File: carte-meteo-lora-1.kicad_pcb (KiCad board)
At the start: 2 copper layers, 118 parts, among them J1 TC2030, J2 Conn_01x04, J3 Conn_01x04, J4 Conn_Coaxial, J5 USB_C_Receptacle_USB2.0_14P, J6 Solar_Cell, J7 Conn_01x02, J8 Battery_Cell, Q1 AO4882, Q2 AO4882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

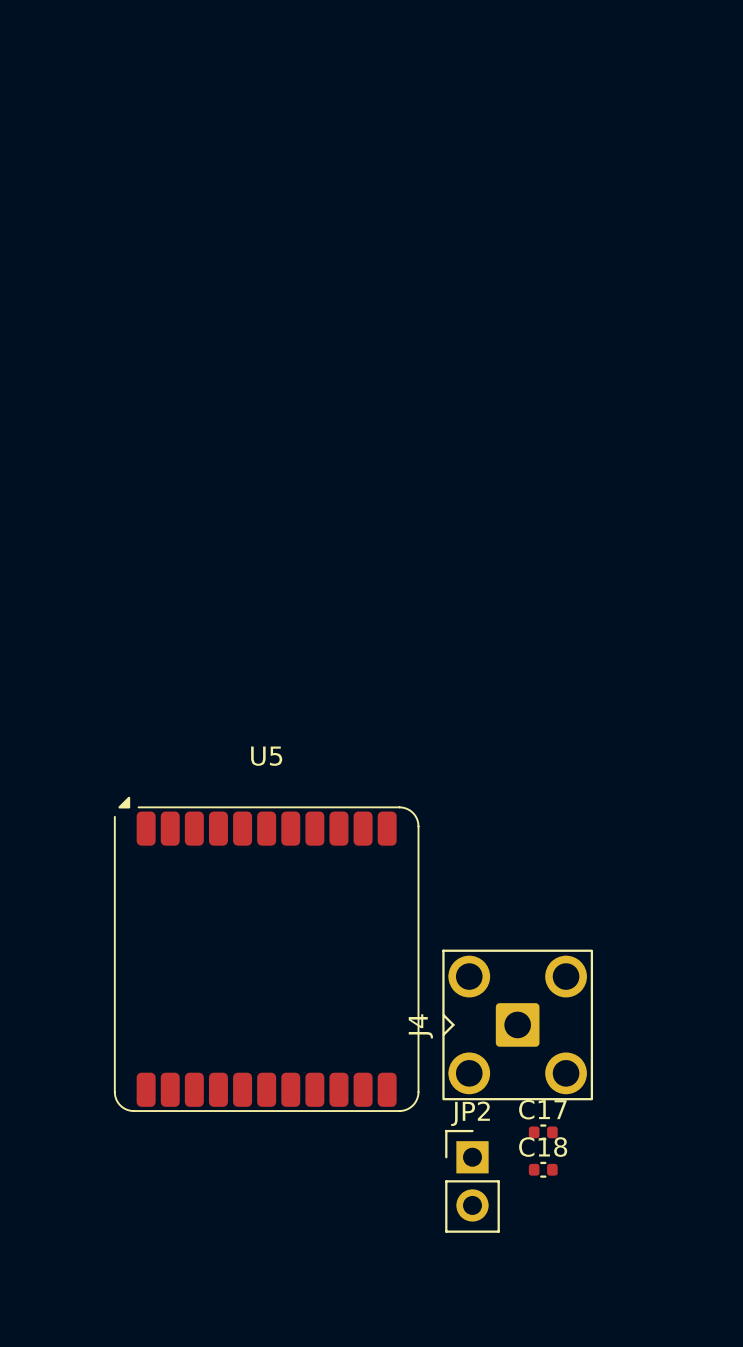
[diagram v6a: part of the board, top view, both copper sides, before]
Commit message: pcb: add lora layout
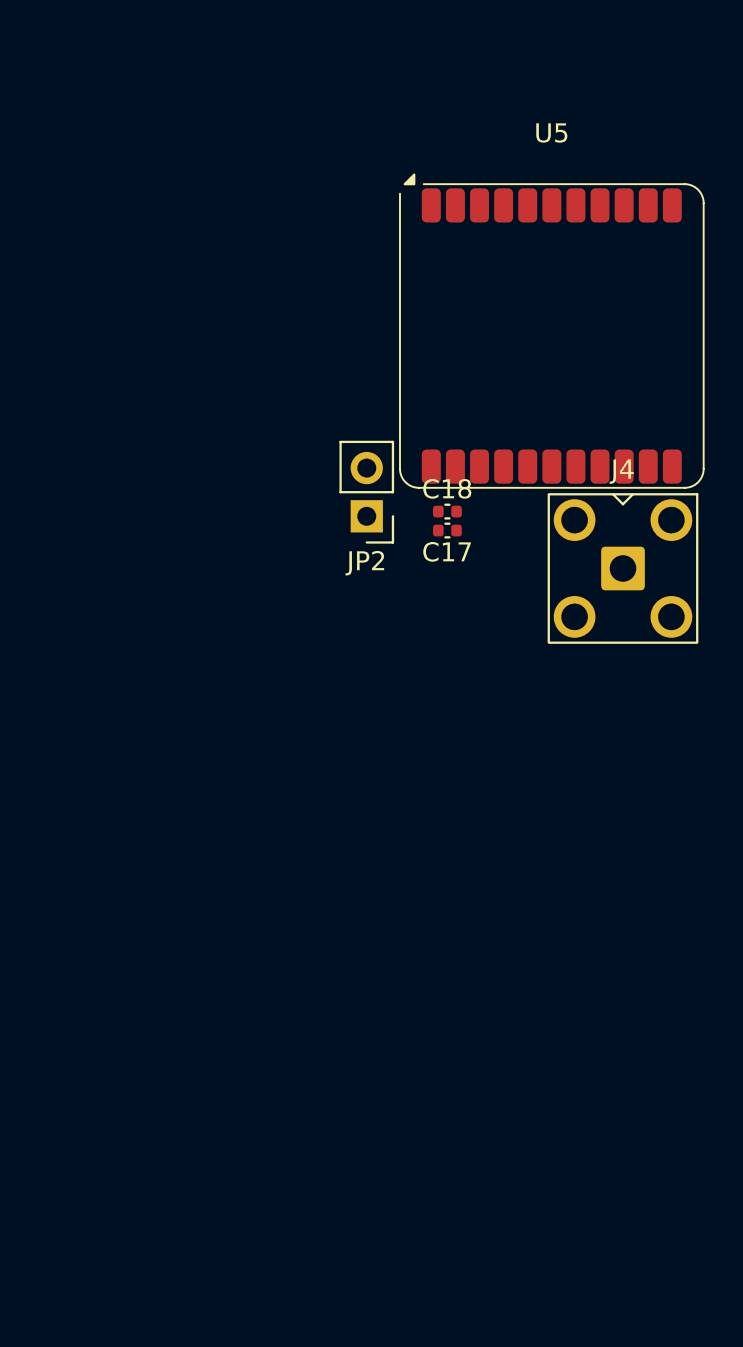
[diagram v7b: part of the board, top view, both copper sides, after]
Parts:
- moved U5 36.1 mm to (199.2, 82.2)
- moved C18 35.0 mm to (193.8, 91.5)
- moved JP2 34.2 mm to (189.5, 91.8), turned to 180 degrees
- moved C17 32.1 mm to (193.8, 92.5), turned to 180 degrees
- moved J4 24.7 mm to (203.0, 94.5), turned to -90 degrees
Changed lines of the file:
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@@
 	(footprint "GLCS:Silicontra_SX1262ZTR8"
 		(layer "F.Cu")
-		(at 184.225 115.085)
+		(at 199.25 82.25)
 		(descr "Silicontra SX1262ZTR8 LoRa Module")
 		(tags "LoRa Silicontra SX1262ZTR8")
@@
 	(footprint "Connector_Coaxial:SMA_BAT_Wireless_BWSMA-KWE-Z001"
 		(layer "F.Cu")
-		(at 197.45 118.55)
+		(at 203 94.5 -90)
 		(descr "BAT Wireless BWSMA-KWE-Z00 https://www.lcsc.com/datasheet/lcsc_datasheet_2310171703_BAT-WIRELESS-BWSMA-KWE-Z001_C496551.pdf")
 		(tags "SMA THT Female Jack Horizontal")
 		(property "Reference" "J4"
-			(at -5.2 0 90)
+			(at -5.2 0 0)
 			(layer "F.SilkS")
 			(effects
@@
 		)
 		(property "Value" "Conn_Coaxial"
-			(at 0 5 0)
+			(at 0 5 90)
 			(layer "F.Fab")
 			(effects
@@
 		)
 		(property "Datasheet" ""
-			(at 0 0 0)
+			(at 0 0 270)
 			(unlocked yes)
 			(layer "F.Fab")
@@
 		)
 		(property "Description" "coaxial connector (BNC, SMA, SMB, SMC, Cinch/RCA, LEMO, ...)"
-			(at 0 0 0)
+			(at 0 0 270)
 			(unlocked yes)
 			(layer "F.Fab")
@@
 		)
 		(property "Basic" "Z"
-			(at 0 0 0)
+			(at 0 0 270)
 			(unlocked yes)
 			(layer "F.Fab")
@@
 		)
 		(property "JLCPCB Part #" "C496551"
-			(at 0 0 0)
+			(at 0 0 270)
 			(unlocked yes)
 			(layer "F.Fab")
@@
 		)
 		(property "Manufacturer" "BAT WIRELESS"
-			(at 0 0 0)
+			(at 0 0 270)
 			(unlocked yes)
 			(layer "F.Fab")
@@
 		)
 		(property "Manufacturer Part Number" "BWSMA-KWE-Z001"
-			(at 0 0 0)
+			(at 0 0 270)
 			(unlocked yes)
 			(layer "F.Fab")
@@
 		)
 		(fp_line
-			(start -3 -9.5)
-			(end 3 -10)
+			(start -3 3)
+			(end 3 3)
 			(stroke
 				(width 0.1)
@@
 		)
 		(fp_line
-			(start -3 -9)
-			(end 3 -9.5)
+			(start -2 0)
+			(end -3 1)
 			(stroke
 				(width 0.1)
@@
 		)
 		(fp_line
-			(start -3 -8.5)
-			(end 3 -9)
+			(start -3 -1)
+			(end -2 0)
 			(stroke
 				(width 0.1)
@@
 		)
 		(fp_line
-			(start -3 -8)
-			(end 3 -8.5)
+			(start -3 -3)
+			(end -3 3)
 			(stroke
 				(width 0.1)
@@
 		)
 		(fp_line
-			(start -3 -7.5)
-			(end 3 -8)
+			(start -3 -3)
+			(end 3 -3)
 			(stroke
 				(width 0.1)
@@
 		)
 		(fp_line
-			(start -3 -7)
-			(end 3 -7.5)
+			(start 3 -3)
+			(end 3 3)
 			(stroke
 				(width 0.1)
@@
 		)
 		(fp_line
-			(start -3 -3)
-			(end -3 3)
+			(start -3 -7)
+			(end 3 -7.5)
 			(stroke
 				(width 0.1)
@@
 		)
 		(fp_line
-			(start -3 -3)
-			(end 3 -3)
+			(start -3 -7.5)
+			(end 3 -8)
 			(stroke
 				(width 0.1)
@@
 		)
 		(fp_line
-			(start -3 -1)
-			(end -2 0)
+			(start -3 -8)
+			(end 3 -8.5)
 			(stroke
 				(width 0.1)
@@
 		)
 		(fp_line
-			(start -3 3)
-			(end 3 3)
+			(start -3 -8.5)
+			(end 3 -9)
 			(stroke
 				(width 0.1)
@@
 		)
 		(fp_line
-			(start -2.5 -11.5)
-			(end -2.5 -3)
+			(start -3 -9)
+			(end 3 -9.5)
 			(stroke
 				(width 0.1)
@@
 		)
 		(fp_line
-			(start -2.5 -11.5)
-			(end 2.5 -11.5)
+			(start -3 -9.5)
+			(end 3 -10)
 			(stroke
 				(width 0.1)
@@
 		)
 		(fp_line
-			(start -2 0)
-			(end -3 1)
+			(start -2.5 -11.5)
+			(end -2.5 -3)
 			(stroke
 				(width 0.1)
@@
 		)
 		(fp_line
-			(start 2.5 -11.5)
-			(end 2.5 -3)
+			(start -2.5 -11.5)
+			(end 2.5 -11.5)
 			(stroke
 				(width 0.1)
@@
 		)
 		(fp_line
-			(start 3 -3)
-			(end 3 3)
+			(start 2.5 -11.5)
+			(end 2.5 -3)
 			(stroke
 				(width 0.1)
@@
 		)
 		(fp_text user "${REFERENCE}"
-			(at 0 0 0)
+			(at 0 0 90)
 			(layer "F.Fab")
 			(effects
@@
 		)
 		(pad "1" thru_hole roundrect
-			(at 0 0)
+			(at 0 0 270)
 			(size 2.3 2.3)
 			(drill 1.4)
@@
 		)
 		(pad "2" thru_hole circle
-			(at -2.55 -2.55)
+			(at -2.55 -2.55 270)
 			(size 2.2 2.2)
 			(drill 1.4)
@@
 		)
 		(pad "2" thru_hole circle
-			(at -2.55 2.55)
+			(at -2.55 2.55 270)
 			(size 2.2 2.2)
 			(drill 1.4)
@@
 		)
 		(pad "2" thru_hole circle
-			(at 2.55 -2.55)
+			(at 2.55 -2.55 270)
 			(size 2.2 2.2)
 			(drill 1.4)
@@
 		)
 		(pad "2" thru_hole circle
-			(at 2.55 2.55)
+			(at 2.55 2.55 270)
 			(size 2.2 2.2)
 			(drill 1.4)
@@
 	(footprint "Capacitor_SMD:C_0402_1005Metric"
 		(layer "F.Cu")
-		(at 198.8 124.21)
+		(at 193.75 92.5 180)
 		(descr "Capacitor SMD 0402 (1005 Metric), square (rectangular) end terminal, IPC-7351 nominal, (Body size source: IPC-SM-782 page 76, https://www.pcb-3d.com/wordpress/wp-content/uploads/ipc-sm-782a_amendment_1_and_2.pdf)")
 		(tags "capacitor")
@@
 		)
 		(property "Manufacturer" "Samsung Electro-Mechanics "
-			(at 0 0 0)
+			(at 0 0 180)
 			(unlocked yes)
 			(layer "F.Fab")
@@
 		)
 		(property "Manufacturer Part Number" "CL05A106MQ5NUNC"
-			(at 0 0 0)
+			(at 0 0 180)
 			(unlocked yes)
 			(layer "F.Fab")
@@
 		)
 		(property "Basic" "Y"
-			(at 0 0 0)
+			(at 0 0 180)
 			(unlocked yes)
 			(layer "F.Fab")
@@
 		)
 		(property "JLCPCB Part #" "C15525"
-			(at 0 0 0)
+			(at 0 0 180)
 			(unlocked yes)
 			(layer "F.Fab")
@@
 		(duplicate_pad_numbers_are_jumpers no)
 		(fp_line
-			(start -0.107836 -0.36)
-			(end 0.107836 -0.36)
+			(start -0.107836 0.36)
+			(end 0.107836 0.36)
 			(stroke
 				(width 0.12)
@@
 		)
 		(fp_line
-			(start -0.107836 0.36)
-			(end 0.107836 0.36)
+			(start -0.107836 -0.36)
+			(end 0.107836 -0.36)
 			(stroke
 				(width 0.12)
@@
 		)
 		(pad "1" smd roundrect
-			(at -0.48 0)
+			(at -0.48 0 180)
 			(size 0.56 0.62)
 			(layers "F.Cu" "F.Mask" "F.Paste")
@@
 		)
 		(pad "2" smd roundrect
-			(at 0.48 0)
+			(at 0.48 0 180)
 			(size 0.56 0.62)
 			(layers "F.Cu" "F.Mask" "F.Paste")
@@
 	(footprint "Capacitor_SMD:C_0402_1005Metric"
 		(layer "F.Cu")
-		(at 198.8 126.18)
+		(at 193.75 91.5)
 		(descr "Capacitor SMD 0402 (1005 Metric), square (rectangular) end terminal, IPC-7351 nominal, (Body size source: IPC-SM-782 page 76, https://www.pcb-3d.com/wordpress/wp-content/uploads/ipc-sm-782a_amendment_1_and_2.pdf)")
 		(tags "capacitor")
@@
 	(footprint "Connector_PinHeader_2.54mm:PinHeader_1x02_P2.54mm_Vertical"
 		(layer "F.Cu")
-		(at 195.07 125.52)
+		(at 189.5 91.75 180)
 		(descr "Through hole straight pin header, 1x02, 2.54mm pitch, single row")
 		(tags "Through hole pin header THT 1x02 2.54mm single row")
@@
 		)
 		(fp_line
-			(start -1.38 -1.38)
-			(end 0 -1.38)
+			(start 1.38 1.27)
+			(end 1.38 3.92)
 			(stroke
 				(width 0.12)
@@
 		)
 		(fp_line
-			(start -1.38 0)
-			(end -1.38 -1.38)
+			(start -1.38 3.92)
+			(end 1.38 3.92)
 			(stroke
 				(width 0.12)
@@
 		(fp_line
 			(start -1.38 1.27)
-			(end -1.38 3.92)
+			(end 1.38 1.27)
 			(stroke
 				(width 0.12)
@@
 		(fp_line
 			(start -1.38 1.27)
-			(end 1.38 1.27)
+			(end -1.38 3.92)
 			(stroke
 				(width 0.12)
@@
 		)
 		(fp_line
-			(start -1.38 3.92)
-			(end 1.38 3.92)
+			(start -1.38 0)
+			(end -1.38 -1.38)
 			(stroke
 				(width 0.12)
@@
 		)
 		(fp_line
-			(start 1.38 1.27)
-			(end 1.38 3.92)
+			(start -1.38 -1.38)
+			(end 0 -1.38)
 			(stroke
 				(width 0.12)
@@
 		)
 		(fp_line
-			(start -1.27 -0.635)
-			(end -0.635 -1.27)
+			(start 1.27 3.81)
+			(end -1.27 3.81)
 			(stroke
 				(width 0.1)
@@
 		)
 		(fp_line
-			(start -1.27 3.81)
-			(end -1.27 -0.635)
+			(start 1.27 -1.27)
+			(end 1.27 3.81)
 			(stroke
 				(width 0.1)
@@
 		)
 		(fp_line
-			(start 1.27 -1.27)
-			(end 1.27 3.81)
+			(start -1.27 3.81)
+			(end -1.27 -0.635)
 			(stroke
 				(width 0.1)
@@
 		)
 		(fp_line
-			(start 1.27 3.81)
-			(end -1.27 3.81)
+			(start -1.27 -0.635)
+			(end -0.635 -1.27)
 			(stroke
 				(width 0.1)
@@
 		)
 		(pad "1" thru_hole rect
-			(at 0 0)
+			(at 0 0 180)
 			(size 1.7 1.7)
 			(drill 1)
@@
 		)
 		(pad "2" thru_hole circle
-			(at 0 2.54)
+			(at 0 2.54 180)
 			(size 1.7 1.7)
 			(drill 1)

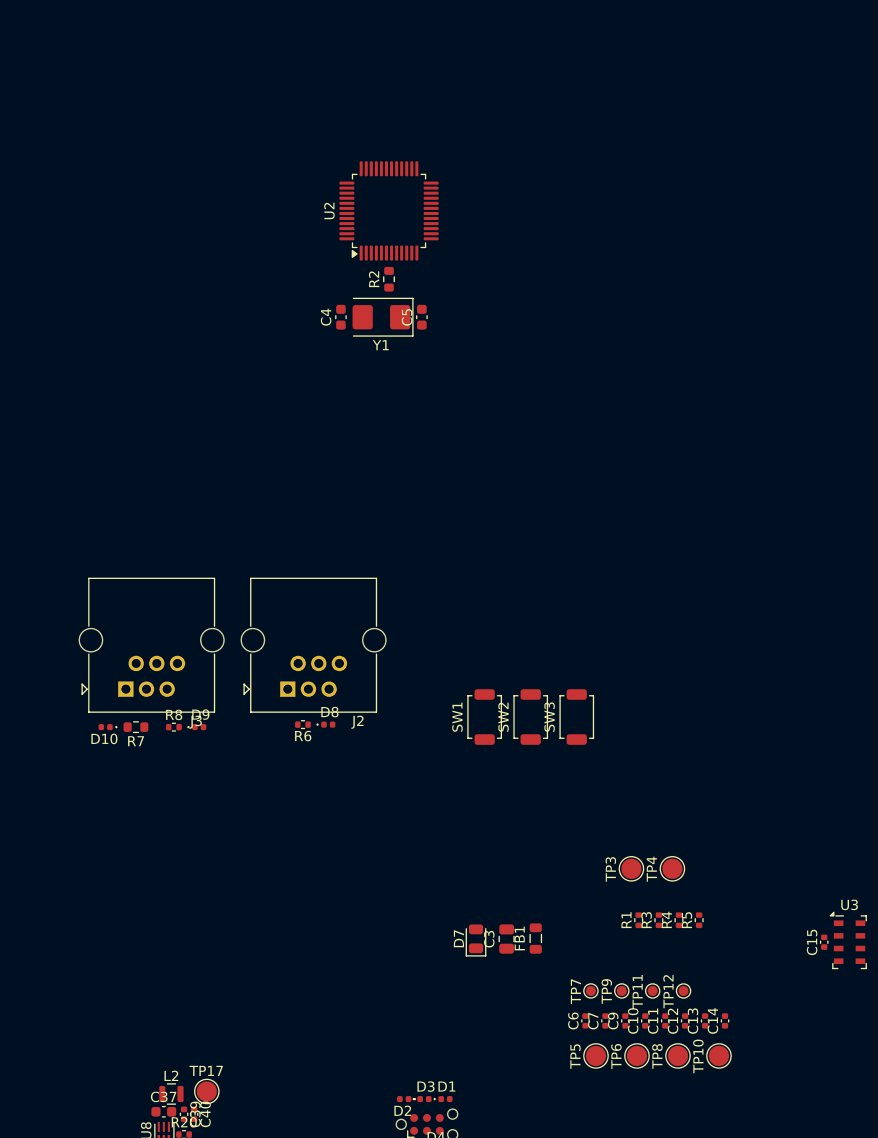
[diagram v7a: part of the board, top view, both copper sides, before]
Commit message: pcb: add stm32 layout
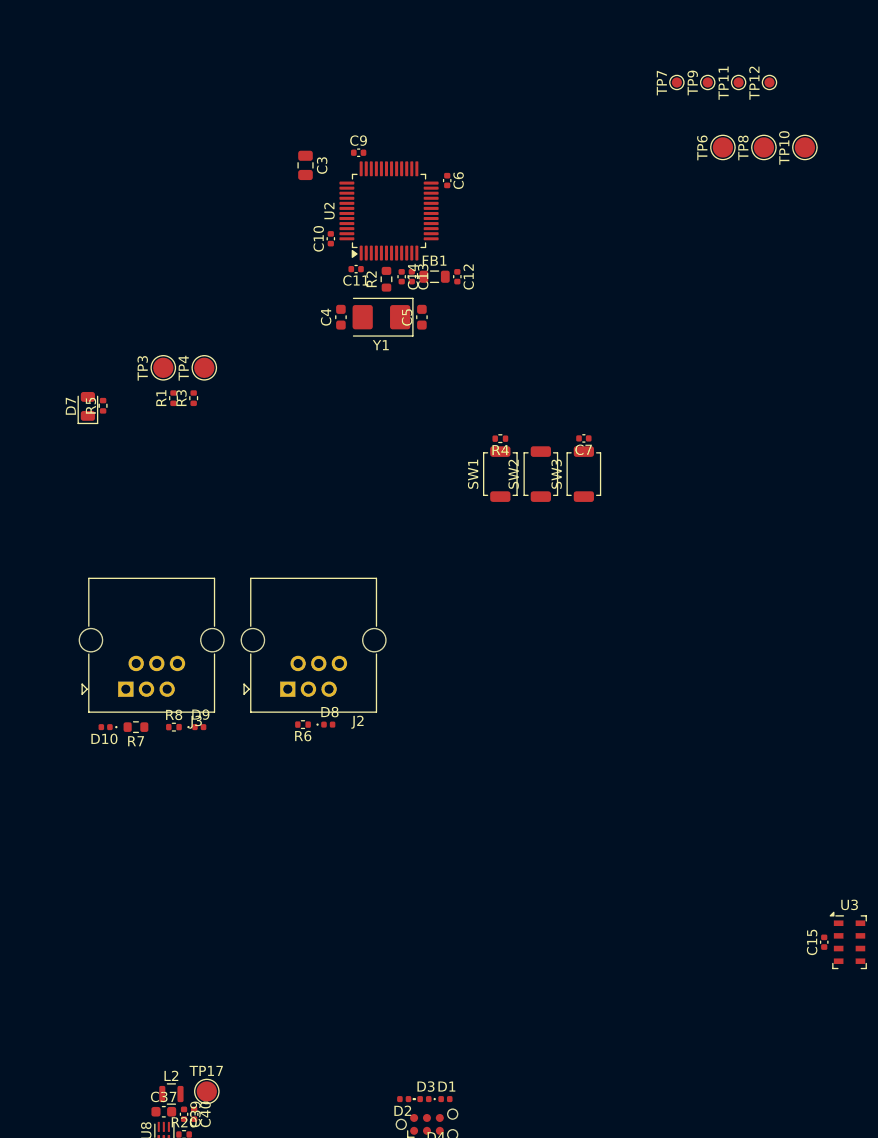
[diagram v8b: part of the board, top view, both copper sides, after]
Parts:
- removed TP5: TestPoint, TestPoint:TestPoint_Pad_D2.0mm
- moved TP10 90.2 mm to (179.1, 62.7)
- moved TP6 90.2 mm to (171.0, 62.7)
- moved TP8 90.2 mm to (175.0, 62.7)
- moved TP11 90.2 mm to (172.5, 56.3)
- moved TP12 90.2 mm to (175.6, 56.3)
- moved TP7 90.2 mm to (166.4, 56.3)
- moved TP9 90.2 mm to (169.5, 56.3)
- moved C9 89.7 mm to (135.0, 63.2), turned to 0 degrees
- moved C6 84.1 mm to (143.8, 66.0), turned to -90 degrees
- moved C10 83.3 mm to (132.2, 71.8)
- moved C11 80.3 mm to (134.8, 74.8), turned to 180 degrees
- moved C14 80.2 mm to (139.2, 75.5), turned to -90 degrees
- moved C13 79.0 mm to (140.2, 75.5), turned to -90 degrees
- moved C3 79.0 mm to (129.8, 64.5), turned to -90 degrees
- moved R5 77.8 mm to (109.8, 88.2)
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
